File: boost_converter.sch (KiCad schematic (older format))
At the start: 12 parts

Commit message: small updates
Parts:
- removed R?: R, symbol R
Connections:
- net Control_OUT1 renamed Control_OUT
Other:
- moved on the sheet: R?
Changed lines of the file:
@@
 LIBS:power
 LIBS:device
-LIBS:switches
-LIBS:relays
-LIBS:motors
-LIBS:transistors
-LIBS:conn
 LIBS:linear
 LIBS:regul
-LIBS:74xx
-LIBS:cmos4000
 LIBS:adc-dac
 LIBS:memory
@@
 LIBS:digital-audio
 LIBS:philips
-LIBS:display
 LIBS:cypress
 LIBS:siliconi
@@
 LIBS:atmel
 LIBS:contrib
-LIBS:valves
 LIBS:lakotamm-microprocessors
 LIBS:lakotamm-powersupply
@@
 LIBS:lakotamm-transistor
 LIBS:lakotamm-wireless
+LIBS:MCU_ST_STM32
+LIBS:Transistor
+LIBS:Connector
 LIBS:F3K_Battery_manager-cache
 EELAYER 25 0
@@
 $EndComp
 Wire Wire Line
-	5850 4450 5850 4550
+	5850 4450 5850 4500
+Wire Wire Line
+	5850 4500 5850 4550
 Wire Wire Line
 	5750 4450 5750 4500
@@
 	6850 4150 6850 4200
 Wire Wire Line
-	6850 3750 6850 3850
+	6850 3750 6850 3800
+Wire Wire Line
+	6850 3800 6850 3850
 Wire Wire Line
 	6850 3350 6850 3450
 Wire Wire Line
-	6400 3350 8300 3350
+	6400 3350 6550 3350
+Wire Wire Line
+	6550 3350 6850 3350
+Wire Wire Line
+	6850 3350 8200 3350
+Wire Wire Line
+	8200 3350 8300 3350
 Connection ~ 6850 3800
 Wire Wire Line
@@
 Connection ~ 8200 3350
 Wire Wire Line
-	3650 3550 5200 3550
+	3650 3550 3800 3550
+Wire Wire Line
+	3800 3550 4550 3550
+Wire Wire Line
+	4550 3550 4850 3550
+Wire Wire Line
+	4850 3550 5200 3550
 Wire Wire Line
 	3800 3550 3800 3700
@@
 	4850 3900 4850 3950
 Wire Wire Line
-	4650 3950 5200 3950
+	4650 3950 4850 3950
+Wire Wire Line
+	4850 3950 5200 3950
 $Comp
 L R R?
 U 1 1 5AA41C36
-P 7200 3600
-F 0 "R?" V 7280 3600 50  0000 C CNN
-F 1 "R" V 7200 3600 50  0000 C CNN
-F 2 "" V 7130 3600 50  0001 C CNN
-F 3 "" H 7200 3600 50  0001 C CNN
-	1    7200 3600
-	0    1    1    0
-$EndComp
-$Comp
-L R R?
-U 1 1 5AA41D55
 P 7200 3800
 F 0 "R?" V 7280 3800 50  0000 C CNN
@@
 $EndComp
 Wire Wire Line
-	7050 3600 7000 3600
-Wire Wire Line
-	7000 3600 7000 4000
-Wire Wire Line
-	6400 3800 7050 3800
-Text HLabel 7400 3600 2    60   Input ~ 0
-Control_OUT1
+	7050 3800 7000 3800
+Wire Wire Line
+	7000 3800 7000 3800
+Wire Wire Line
+	7000 3800 7000 4000
 Text HLabel 7400 3800 2    60   Input ~ 0
-Control_OUT2
+Control_OUT
 Wire Wire Line
 	7350 3800 7400 3800
-Wire Wire Line
-	7350 3600 7400 3600
 Text HLabel 4650 3950 0    60   Input ~ 0
 ENA
@@
 $EndComp
 Wire Wire Line
-	4650 4100 5200 4100
+	4650 4100 4750 4100
+Wire Wire Line
+	4750 4100 5000 4100
+Wire Wire Line
+	5000 4100 5200 4100
 Wire Wire Line
 	5000 4100 5000 4200
@@
 Wire Wire Line
 	7000 4000 7400 4000
+Wire Wire Line
+	6400 3800 6550 3800
+Wire Wire Line
+	6550 3800 6850 3800
+Wire Wire Line
+	6850 3800 7000 3800
 $EndSCHEMATC

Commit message: added few MPNs
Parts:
- C15: renamed from C?; value 15uF -> 15uF 4V; footprint (none) -> Capacitors_SMD:C_0603; MPN (none) -> C1608X5R0G156M080AA
- C18: renamed from C?; value 33uF -> 33uF 4V; MPN (none) -> GRM21BR60G336ME15L
- L1: renamed from L?; MPN (none) -> IHLP1212BZER1R0M11
- R10: renamed from R?; value R -> 1M
- gave numbers to parts that had none: 7
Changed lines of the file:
@@
 $EndDescr
 $Comp
-L TPS61236P U?
+L TPS61236P U4
 U 1 1 5AA40BBB
 P 5800 3650
-F 0 "U?" H 6150 4100 60  0000 C CNN
+F 0 "U4" H 6150 4100 60  0000 C CNN
 F 1 "TPS61236P" H 5600 4100 60  0000 C CNN
 F 2 "" H 6050 4000 60  0001 C CNN
@@
 $EndComp
 $Comp
-L L L?
+L L L1
 U 1 1 5AA40C48
 P 4850 3350
-F 0 "L?" V 4800 3350 50  0000 C CNN
+F 0 "L1" V 4800 3350 50  0000 C CNN
 F 1 "1.2 uH 18mOhm" V 4925 3350 50  0000 C CNN
 F 2 "" H 4850 3350 50  0001 C CNN
 F 3 "" H 4850 3350 50  0001 C CNN
+F 4 "IHLP1212BZER1R0M11" V 4850 3350 60  0001 C CNN "MPN"
 	1    4850 3350
 	0    -1   -1   0
@@
 NoConn ~ 6400 4100
 $Comp
-L C C?
+L C C17
 U 1 1 5AA40CF8
 P 6550 3550
-F 0 "C?" H 6575 3650 50  0000 L CNN
+F 0 "C17" H 6575 3650 50  0000 L CNN
 F 1 "10pF" H 6575 3450 50  0000 L CNN
 F 2 "" H 6588 3400 50  0001 C CNN
@@
 $EndComp
 $Comp
-L R R?
+L R R11
 U 1 1 5AA40DAF
 P 6850 3600
-F 0 "R?" V 6930 3600 50  0000 C CNN
+F 0 "R11" V 6930 3600 50  0000 C CNN
 F 1 "R" V 6850 3600 50  0000 C CNN
 F 2 "" V 6780 3600 50  0001 C CNN
@@
 $EndComp
 $Comp
-L R R?
+L R R12
 U 1 1 5AA40DF4
 P 6850 4000
-F 0 "R?" V 6930 4000 50  0000 C CNN
+F 0 "R12" V 6930 4000 50  0000 C CNN
 F 1 "R" V 6850 4000 50  0000 C CNN
 F 2 "" V 6780 4000 50  0001 C CNN
@@
 $EndComp
 $Comp
-L GND #PWR?
+L GND #PWR49
 U 1 1 5AA40E28
 P 6850 4200
-F 0 "#PWR?" H 6850 3950 50  0001 C CNN
+F 0 "#PWR49" H 6850 3950 50  0001 C CNN
 F 1 "GND" H 6850 4050 50  0000 C CNN
 F 2 "" H 6850 4200 50  0001 C CNN
@@
 $EndComp
 $Comp
-L GND #PWR?
+L GND #PWR48
 U 1 1 5AA40E49
 P 5850 4550
-F 0 "#PWR?" H 5850 4300 50  0001 C CNN
+F 0 "#PWR48" H 5850 4300 50  0001 C CNN
 F 1 "GND" H 5850 4400 50  0000 C CNN
 F 2 "" H 5850 4550 50  0001 C CNN
@@
 $EndComp
 $Comp
-L C C?
+L C C18
 U 1 1 5AA40FA0
 P 8200 3800
-F 0 "C?" H 8225 3900 50  0000 L CNN
-F 1 "33uF" H 8225 3700 50  0000 L CNN
+F 0 "C18" H 8225 3900 50  0000 L CNN
+F 1 "33uF 4V" H 8250 3700 50  0000 L CNN
 F 2 "" H 8238 3650 50  0001 C CNN
 F 3 "" H 8200 3800 50  0001 C CNN
+F 4 "GRM21BR60G336ME15L" H 8200 3800 60  0001 C CNN "MPN"
 	1    8200 3800
 	1    0    0    -1
 $EndComp
 $Comp
-L GND #PWR?
+L GND #PWR50
 U 1 1 5AA40FE1
 P 8200 4200
-F 0 "#PWR?" H 8200 3950 50  0001 C CNN
+F 0 "#PWR50" H 8200 3950 50  0001 C CNN
 F 1 "GND" H 8200 4050 50  0000 C CNN
 F 2 "" H 8200 4200 50  0001 C CNN
@@
 VOUT
 $Comp
-L C C?
+L C C15
 U 1 1 5AA411D9
 P 3800 3850
-F 0 "C?" H 3825 3950 50  0000 L CNN
-F 1 "15uF" H 3825 3750 50  0000 L CNN
-F 2 "" H 3838 3700 50  0001 C CNN
+F 0 "C15" H 3825 3950 50  0000 L CNN
+F 1 "15uF 4V" H 3825 3750 50  0000 L CNN
+F 2 "Capacitors_SMD:C_0603" H 3838 3700 50  0001 C CNN
 F 3 "" H 3800 3850 50  0001 C CNN
+F 4 "C1608X5R0G156M080AA" H 3800 3850 60  0001 C CNN "MPN"
 	1    3800 3850
 	1    0    0    -1
 $EndComp
 $Comp
-L GND #PWR?
+L GND #PWR45
 U 1 1 5AA412DC
 P 3800 4200
-F 0 "#PWR?" H 3800 3950 50  0001 C CNN
+F 0 "#PWR45" H 3800 3950 50  0001 C CNN
 F 1 "GND" H 3800 4050 50  0000 C CNN
 F 2 "" H 3800 4200 50  0001 C CNN
@@
 $EndComp
 $Comp
-L R R?
+L R R10
 U 1 1 5AA417A7
 P 4850 3750
-F 0 "R?" V 4930 3750 50  0000 C CNN
-F 1 "R" V 4850 3750 50  0000 C CNN
+F 0 "R10" V 4930 3750 50  0000 C CNN
+F 1 "1M" V 4850 3750 50  0000 C CNN
 F 2 "" V 4780 3750 50  0001 C CNN
 F 3 "" H 4850 3750 50  0001 C CNN
@@
 $EndComp
 Wire Wire Line
-	5850 4450 5850 4500
-Wire Wire Line
-	5850 4500 5850 4550
+	5850 4450 5850 4550
 Wire Wire Line
 	5750 4450 5750 4500
@@
 	6850 4150 6850 4200
 Wire Wire Line
-	6850 3750 6850 3800
-Wire Wire Line
-	6850 3800 6850 3850
+	6850 3750 6850 3850
 Wire Wire Line
 	6850 3350 6850 3450
 Wire Wire Line
-	6400 3350 6550 3350
-Wire Wire Line
-	6550 3350 6850 3350
-Wire Wire Line
-	6850 3350 8200 3350
-Wire Wire Line
-	8200 3350 8300 3350
+	6400 3350 8300 3350
 Connection ~ 6850 3800
 Wire Wire Line
@@
 Connection ~ 8200 3350
 Wire Wire Line
-	3650 3550 3800 3550
-Wire Wire Line
-	3800 3550 4550 3550
-Wire Wire Line
-	4550 3550 4850 3550
-Wire Wire Line
-	4850 3550 5200 3550
+	3650 3550 5200 3550
 Wire Wire Line
 	3800 3550 3800 3700
@@
 	4850 3900 4850 3950
 Wire Wire Line
-	4650 3950 4850 3950
-Wire Wire Line
-	4850 3950 5200 3950
-$Comp
-L R R?
+	4650 3950 5200 3950
+$Comp
+L R R13
 U 1 1 5AA41C36
 P 7200 3800
-F 0 "R?" V 7280 3800 50  0000 C CNN
+F 0 "R13" V 7280 3800 50  0000 C CNN
 F 1 "R" V 7200 3800 50  0000 C CNN
 F 2 "" V 7130 3800 50  0001 C CNN
@@
 $EndComp
 Wire Wire Line
-	7050 3800 7000 3800
-Wire Wire Line
-	7000 3800 7000 3800
+	6400 3800 7050 3800
 Wire Wire Line
 	7000 3800 7000 4000
@@
 Connection ~ 4850 3950
 $Comp
-L +BATT #PWR?
+L +BATT #PWR44
 U 1 1 5AA423A0
 P 3650 3450
-F 0 "#PWR?" H 3650 3300 50  0001 C CNN
+F 0 "#PWR44" H 3650 3300 50  0001 C CNN
 F 1 "+BATT" H 3650 3590 50  0000 C CNN
 F 2 "" H 3650 3450 50  0001 C CNN
@@
 Connection ~ 3800 3550
 $Comp
-L C C?
+L C C16
 U 1 1 5AA42591
 P 5000 4350
-F 0 "C?" H 5025 4450 50  0000 L CNN
+F 0 "C16" H 5025 4450 50  0000 L CNN
 F 1 "10nF" H 5025 4250 50  0000 L CNN
 F 2 "" H 5038 4200 50  0001 C CNN
@@
 $EndComp
 $Comp
-L R R?
+L R R9
 U 1 1 5AA425EF
 P 4750 4350
-F 0 "R?" V 4830 4350 50  0000 C CNN
+F 0 "R9" V 4830 4350 50  0000 C CNN
 F 1 "R" V 4750 4350 50  0000 C CNN
 F 2 "" V 4680 4350 50  0001 C CNN
@@
 $EndComp
 Wire Wire Line
-	4650 4100 4750 4100
-Wire Wire Line
-	4750 4100 5000 4100
-Wire Wire Line
-	5000 4100 5200 4100
+	4650 4100 5200 4100
 Wire Wire Line
 	5000 4100 5000 4200
@@
 Connection ~ 5000 4100
 $Comp
-L GND #PWR?
+L GND #PWR47
 U 1 1 5AA42711
 P 5000 4550
-F 0 "#PWR?" H 5000 4300 50  0001 C CNN
+F 0 "#PWR47" H 5000 4300 50  0001 C CNN
 F 1 "GND" H 5000 4400 50  0000 C CNN
 F 2 "" H 5000 4550 50  0001 C CNN
@@
 	5000 4500 5000 4550
 $Comp
-L GND #PWR?
+L GND #PWR46
 U 1 1 5AA42804
 P 4750 4550
-F 0 "#PWR?" H 4750 4300 50  0001 C CNN
+F 0 "#PWR46" H 4750 4300 50  0001 C CNN
 F 1 "GND" H 4750 4400 50  0000 C CNN
 F 2 "" H 4750 4550 50  0001 C CNN
@@
 Wire Wire Line
 	7000 4000 7400 4000
-Wire Wire Line
-	6400 3800 6550 3800
-Wire Wire Line
-	6550 3800 6850 3800
-Wire Wire Line
-	6850 3800 7000 3800
 $EndSCHEMATC

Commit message: Progress on the charging circuit
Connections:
- net Control_OUT renamed Voltage_control
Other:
- moved on the sheet: C18
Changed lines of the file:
@@
 $Descr A4 11693 8268
 encoding utf-8
-Sheet 4 4
+Sheet 3 4
 Title ""
 Date ""
@@
 L C C18
 U 1 1 5AA40FA0
-P 8200 3800
-F 0 "C18" H 8225 3900 50  0000 L CNN
-F 1 "33uF 4V" H 8250 3700 50  0000 L CNN
-F 2 "" H 8238 3650 50  0001 C CNN
-F 3 "" H 8200 3800 50  0001 C CNN
-F 4 "GRM21BR60G336ME15L" H 8200 3800 60  0001 C CNN "MPN"
-	1    8200 3800
+P 8300 3800
+F 0 "C18" H 8325 3900 50  0000 L CNN
+F 1 "33uF 4V" H 8350 3700 50  0000 L CNN
+F 2 "" H 8338 3650 50  0001 C CNN
+F 3 "" H 8300 3800 50  0001 C CNN
+F 4 "GRM21BR60G336ME15L" H 8300 3800 60  0001 C CNN "MPN"
+	1    8300 3800
 	1    0    0    -1
 $EndComp
@@
 L GND #PWR50
 U 1 1 5AA40FE1
-P 8200 4200
-F 0 "#PWR50" H 8200 3950 50  0001 C CNN
-F 1 "GND" H 8200 4050 50  0000 C CNN
-F 2 "" H 8200 4200 50  0001 C CNN
-F 3 "" H 8200 4200 50  0001 C CNN
-	1    8200 4200
-	1    0    0    -1
-$EndComp
-Text HLabel 8300 3350 2    60   Output ~ 0
+P 8300 4200
+F 0 "#PWR50" H 8300 3950 50  0001 C CNN
+F 1 "GND" H 8300 4050 50  0000 C CNN
+F 2 "" H 8300 4200 50  0001 C CNN
+F 3 "" H 8300 4200 50  0001 C CNN
+	1    8300 4200
+	1    0    0    -1
+$EndComp
+Text HLabel 8400 3350 2    60   Output ~ 0
 VOUT
 $Comp
@@
 $EndComp
 Wire Wire Line
-	5850 4450 5850 4550
+	5850 4450 5850 4500
+Wire Wire Line
+	5850 4500 5850 4550
 Wire Wire Line
 	5750 4450 5750 4500
@@
 	6850 4150 6850 4200
 Wire Wire Line
-	6850 3750 6850 3850
+	6850 3750 6850 3800
+Wire Wire Line
+	6850 3800 6850 3850
 Wire Wire Line
 	6850 3350 6850 3450
 Wire Wire Line
-	6400 3350 8300 3350
+	6400 3350 6550 3350
+Wire Wire Line
+	6550 3350 6850 3350
+Wire Wire Line
+	6850 3350 8300 3350
+Wire Wire Line
+	8300 3350 8400 3350
 Connection ~ 6850 3800
 Wire Wire Line
@@
 Connection ~ 6550 3350
 Wire Wire Line
-	8200 3350 8200 3650
+	8300 3350 8300 3650
 Connection ~ 6850 3350
 Wire Wire Line
-	8200 3950 8200 4200
-Connection ~ 8200 3350
-Wire Wire Line
-	3650 3550 5200 3550
+	8300 3950 8300 4200
+Connection ~ 8300 3350
+Wire Wire Line
+	3650 3550 3800 3550
+Wire Wire Line
+	3800 3550 4550 3550
+Wire Wire Line
+	4550 3550 4850 3550
+Wire Wire Line
+	4850 3550 5200 3550
 Wire Wire Line
 	3800 3550 3800 3700
@@
 	4850 3900 4850 3950
 Wire Wire Line
-	4650 3950 5200 3950
+	4650 3950 4850 3950
+Wire Wire Line
+	4850 3950 5200 3950
 $Comp
 L R R13
@@
 $EndComp
 Wire Wire Line
-	6400 3800 7050 3800
+	6400 3800 6550 3800
+Wire Wire Line
+	6550 3800 6850 3800
+Wire Wire Line
+	6850 3800 7000 3800
+Wire Wire Line
+	7000 3800 7050 3800
 Wire Wire Line
 	7000 3800 7000 4000
 Text HLabel 7400 3800 2    60   Input ~ 0
-Control_OUT
+Voltage_control
 Wire Wire Line
 	7350 3800 7400 3800
@@
 $EndComp
 Wire Wire Line
-	4650 4100 5200 4100
+	4650 4100 4750 4100
+Wire Wire Line
+	4750 4100 5000 4100
+Wire Wire Line
+	5000 4100 5200 4100
 Wire Wire Line
 	5000 4100 5000 4200

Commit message: Updated MCU pinout
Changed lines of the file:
@@
 $EndComp
 Wire Wire Line
-	5850 4450 5850 4500
-Wire Wire Line
-	5850 4500 5850 4550
+	5850 4450 5850 4550
 Wire Wire Line
 	5750 4450 5750 4500
@@
 	6850 4150 6850 4200
 Wire Wire Line
-	6850 3750 6850 3800
-Wire Wire Line
-	6850 3800 6850 3850
+	6850 3750 6850 3850
 Wire Wire Line
 	6850 3350 6850 3450
 Wire Wire Line
-	6400 3350 6550 3350
-Wire Wire Line
-	6550 3350 6850 3350
-Wire Wire Line
-	6850 3350 8300 3350
-Wire Wire Line
-	8300 3350 8400 3350
+	6400 3350 8400 3350
 Connection ~ 6850 3800
 Wire Wire Line
@@
 Connection ~ 8300 3350
 Wire Wire Line
-	3650 3550 3800 3550
-Wire Wire Line
-	3800 3550 4550 3550
-Wire Wire Line
-	4550 3550 4850 3550
-Wire Wire Line
-	4850 3550 5200 3550
+	3650 3550 5200 3550
 Wire Wire Line
 	3800 3550 3800 3700
@@
 	4850 3900 4850 3950
 Wire Wire Line
-	4650 3950 4850 3950
-Wire Wire Line
-	4850 3950 5200 3950
+	4650 3950 5200 3950
 $Comp
 L R R13
@@
 $EndComp
 Wire Wire Line
-	6400 3800 6550 3800
-Wire Wire Line
-	6550 3800 6850 3800
-Wire Wire Line
-	6850 3800 7000 3800
-Wire Wire Line
-	7000 3800 7050 3800
+	6400 3800 7050 3800
 Wire Wire Line
 	7000 3800 7000 4000
@@
 $EndComp
 Wire Wire Line
-	4650 4100 4750 4100
-Wire Wire Line
-	4750 4100 5000 4100
-Wire Wire Line
-	5000 4100 5200 4100
+	4650 4100 5200 4100
 Wire Wire Line
 	5000 4100 5000 4200

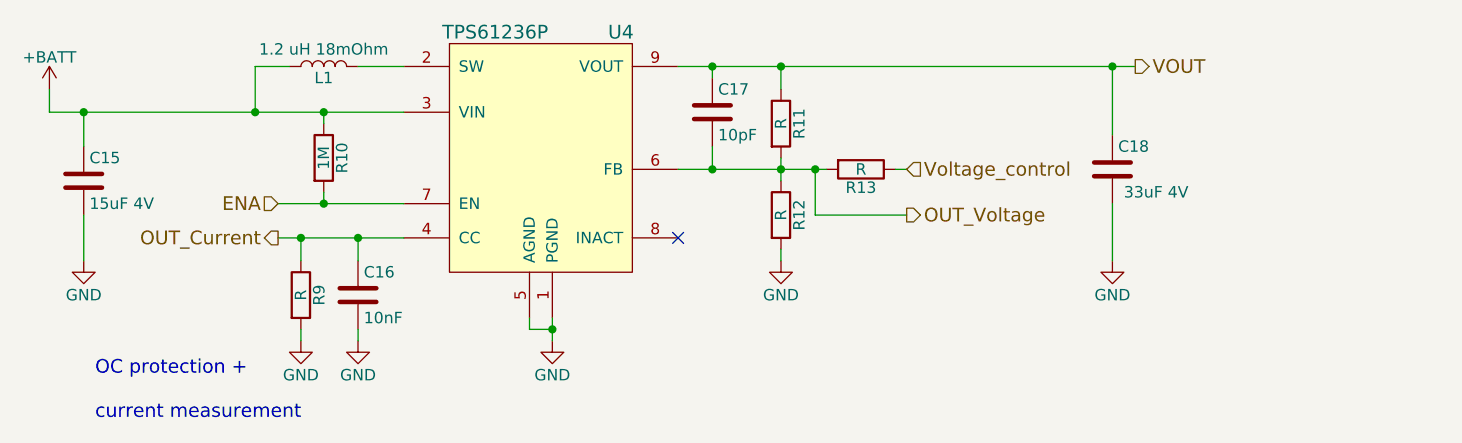
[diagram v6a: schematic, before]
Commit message: Simplified schematic, changed pinout
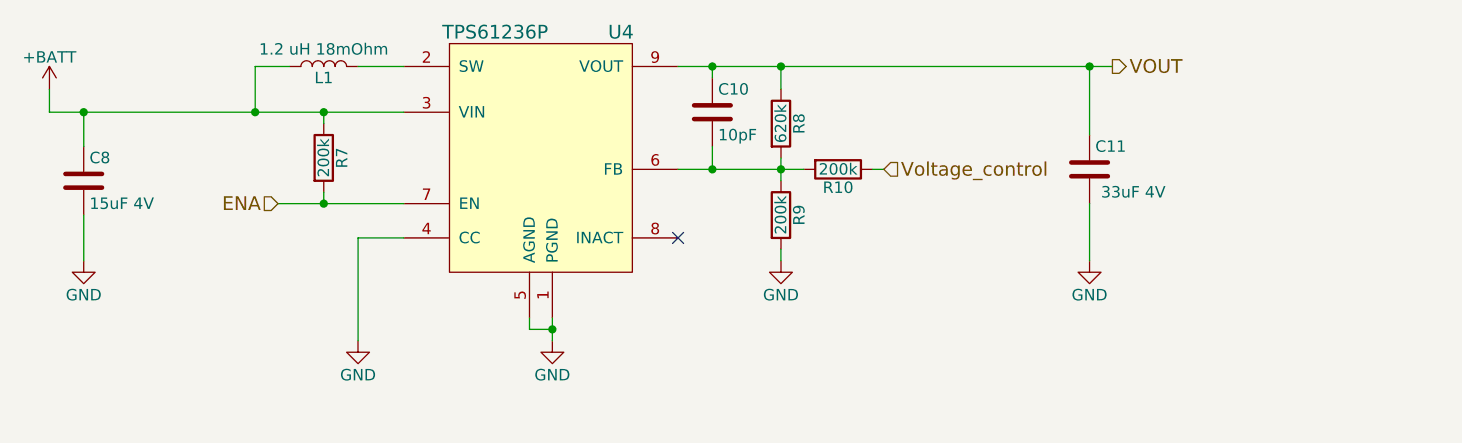
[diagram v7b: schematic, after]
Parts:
- removed C16: 10nF, symbol C
- removed R9: R, symbol R
- R10: renamed from R13; value R -> 200k; footprint (none) -> Resistors_SMD:R_0402
- R7: renamed from R10; value 1M -> 200k; footprint (none) -> Resistors_SMD:R_0402
- R8: renamed from R11; value R -> 620k; footprint (none) -> Resistors_SMD:R_0402
- R9: renamed from R12; value R -> 200k; footprint (none) -> Resistors_SMD:R_0402
- renumbered C17 to C10, C18 to C11, C15 to C8
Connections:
- net OUT_Current is gone; now on net GND: U4.4 (CC)
- net OUT_Voltage: no longer names the net of C10.2, R10.2, R8.2, R9.1, U4.6 (FB)
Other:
- note removed: "OC protection +\n\ncurrent measurement\n"
- moved on the sheet: C11, R10
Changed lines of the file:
@@
 NoConn ~ 6400 4100
 $Comp
-L C C17
+L C C10
 U 1 1 5AA40CF8
 P 6550 3550
-F 0 "C17" H 6575 3650 50  0000 L CNN
+F 0 "C10" H 6575 3650 50  0000 L CNN
 F 1 "10pF" H 6575 3450 50  0000 L CNN
 F 2 "" H 6588 3400 50  0001 C CNN
@@
 $EndComp
 $Comp
-L R R11
+L R R8
 U 1 1 5AA40DAF
 P 6850 3600
-F 0 "R11" V 6930 3600 50  0000 C CNN
-F 1 "R" V 6850 3600 50  0000 C CNN
-F 2 "" V 6780 3600 50  0001 C CNN
+F 0 "R8" V 6930 3600 50  0000 C CNN
+F 1 "620k" V 6850 3600 50  0000 C CNN
+F 2 "Resistors_SMD:R_0402" V 6780 3600 50  0001 C CNN
 F 3 "" H 6850 3600 50  0001 C CNN
 	1    6850 3600
@@
 $EndComp
 $Comp
-L R R12
+L R R9
 U 1 1 5AA40DF4
 P 6850 4000
-F 0 "R12" V 6930 4000 50  0000 C CNN
-F 1 "R" V 6850 4000 50  0000 C CNN
-F 2 "" V 6780 4000 50  0001 C CNN
+F 0 "R9" V 6930 4000 50  0000 C CNN
+F 1 "200k" V 6850 4000 50  0000 C CNN
+F 2 "Resistors_SMD:R_0402" V 6780 4000 50  0001 C CNN
 F 3 "" H 6850 4000 50  0001 C CNN
 	1    6850 4000
@@
 $EndComp
 $Comp
-L GND #PWR49
+L GND #PWR032
 U 1 1 5AA40E28
 P 6850 4200
-F 0 "#PWR49" H 6850 3950 50  0001 C CNN
+F 0 "#PWR032" H 6850 3950 50  0001 C CNN
 F 1 "GND" H 6850 4050 50  0000 C CNN
 F 2 "" H 6850 4200 50  0001 C CNN
@@
 $EndComp
 $Comp
-L GND #PWR48
+L GND #PWR033
 U 1 1 5AA40E49
 P 5850 4550
-F 0 "#PWR48" H 5850 4300 50  0001 C CNN
+F 0 "#PWR033" H 5850 4300 50  0001 C CNN
 F 1 "GND" H 5850 4400 50  0000 C CNN
 F 2 "" H 5850 4550 50  0001 C CNN
@@
 $EndComp
 $Comp
-L C C18
+L C C11
 U 1 1 5AA40FA0
-P 8300 3800
-F 0 "C18" H 8325 3900 50  0000 L CNN
-F 1 "33uF 4V" H 8350 3700 50  0000 L CNN
-F 2 "" H 8338 3650 50  0001 C CNN
-F 3 "" H 8300 3800 50  0001 C CNN
-F 4 "GRM21BR60G336ME15L" H 8300 3800 60  0001 C CNN "MPN"
-	1    8300 3800
-	1    0    0    -1
-$EndComp
-$Comp
-L GND #PWR50
+P 8200 3800
+F 0 "C11" H 8225 3900 50  0000 L CNN
+F 1 "33uF 4V" H 8250 3700 50  0000 L CNN
+F 2 "" H 8238 3650 50  0001 C CNN
+F 3 "" H 8200 3800 50  0001 C CNN
+F 4 "GRM21BR60G336ME15L" H 8200 3800 60  0001 C CNN "MPN"
+	1    8200 3800
+	1    0    0    -1
+$EndComp
+$Comp
+L GND #PWR034
 U 1 1 5AA40FE1
-P 8300 4200
-F 0 "#PWR50" H 8300 3950 50  0001 C CNN
-F 1 "GND" H 8300 4050 50  0000 C CNN
-F 2 "" H 8300 4200 50  0001 C CNN
-F 3 "" H 8300 4200 50  0001 C CNN
-	1    8300 4200
-	1    0    0    -1
-$EndComp
-Text HLabel 8400 3350 2    60   Output ~ 0
+P 8200 4200
+F 0 "#PWR034" H 8200 3950 50  0001 C CNN
+F 1 "GND" H 8200 4050 50  0000 C CNN
+F 2 "" H 8200 4200 50  0001 C CNN
+F 3 "" H 8200 4200 50  0001 C CNN
+	1    8200 4200
+	1    0    0    -1
+$EndComp
+Text HLabel 8300 3350 2    60   Output ~ 0
 VOUT
 $Comp
-L C C15
+L C C8
 U 1 1 5AA411D9
 P 3800 3850
-F 0 "C15" H 3825 3950 50  0000 L CNN
+F 0 "C8" H 3825 3950 50  0000 L CNN
 F 1 "15uF 4V" H 3825 3750 50  0000 L CNN
 F 2 "Capacitors_SMD:C_0603" H 3838 3700 50  0001 C CNN
@@
 $EndComp
 $Comp
-L GND #PWR45
+L GND #PWR035
 U 1 1 5AA412DC
 P 3800 4200
-F 0 "#PWR45" H 3800 3950 50  0001 C CNN
+F 0 "#PWR035" H 3800 3950 50  0001 C CNN
 F 1 "GND" H 3800 4050 50  0000 C CNN
 F 2 "" H 3800 4200 50  0001 C CNN
@@
 $EndComp
 $Comp
-L R R10
+L R R7
 U 1 1 5AA417A7
 P 4850 3750
-F 0 "R10" V 4930 3750 50  0000 C CNN
-F 1 "1M" V 4850 3750 50  0000 C CNN
-F 2 "" V 4780 3750 50  0001 C CNN
+F 0 "R7" V 4930 3750 50  0000 C CNN
+F 1 "200k" V 4850 3750 50  0000 C CNN
+F 2 "Resistors_SMD:R_0402" V 4780 3750 50  0001 C CNN
 F 3 "" H 4850 3750 50  0001 C CNN
 	1    4850 3750
@@
 	6850 3350 6850 3450
 Wire Wire Line
-	6400 3350 8400 3350
+	6400 3350 8300 3350
 Connection ~ 6850 3800
 Wire Wire Line
@@
 Connection ~ 6550 3350
 Wire Wire Line
-	8300 3350 8300 3650
+	8200 3350 8200 3650
 Connection ~ 6850 3350
 Wire Wire Line
-	8300 3950 8300 4200
-Connection ~ 8300 3350
+	8200 3950 8200 4200
+Connection ~ 8200 3350
 Wire Wire Line
 	3650 3550 5200 3550
@@
 	4650 3950 5200 3950
 $Comp
-L R R13
+L R R10
 U 1 1 5AA41C36
-P 7200 3800
-F 0 "R13" V 7280 3800 50  0000 C CNN
-F 1 "R" V 7200 3800 50  0000 C CNN
-F 2 "" V 7130 3800 50  0001 C CNN
-F 3 "" H 7200 3800 50  0001 C CNN
-	1    7200 3800
+P 7100 3800
+F 0 "R10" V 7180 3800 50  0000 C CNN
+F 1 "200k" V 7100 3800 50  0000 C CNN
+F 2 "Resistors_SMD:R_0402" V 7030 3800 50  0001 C CNN
+F 3 "" H 7100 3800 50  0001 C CNN
+	1    7100 3800
 	0    1    1    0
 $EndComp
 Wire Wire Line
-	6400 3800 7050 3800
-Wire Wire Line
-	7000 3800 7000 4000
-Text HLabel 7400 3800 2    60   Input ~ 0
+	6400 3800 6950 3800
+Text HLabel 7300 3800 2    60   Input ~ 0
 Voltage_control
 Wire Wire Line
-	7350 3800 7400 3800
+	7250 3800 7300 3800
 Text HLabel 4650 3950 0    60   Input ~ 0
 ENA
 Connection ~ 4850 3950
 $Comp
-L +BATT #PWR44
+L +BATT #PWR036
 U 1 1 5AA423A0
 P 3650 3450
-F 0 "#PWR44" H 3650 3300 50  0001 C CNN
+F 0 "#PWR036" H 3650 3300 50  0001 C CNN
 F 1 "+BATT" H 3650 3590 50  0000 C CNN
 F 2 "" H 3650 3450 50  0001 C CNN
@@
 Connection ~ 3800 3550
 $Comp
-L C C16
-U 1 1 5AA42591
-P 5000 4350
-F 0 "C16" H 5025 4450 50  0000 L CNN
-F 1 "10nF" H 5025 4250 50  0000 L CNN
-F 2 "" H 5038 4200 50  0001 C CNN
-F 3 "" H 5000 4350 50  0001 C CNN
-	1    5000 4350
-	1    0    0    -1
-$EndComp
-$Comp
-L R R9
-U 1 1 5AA425EF
-P 4750 4350
-F 0 "R9" V 4830 4350 50  0000 C CNN
-F 1 "R" V 4750 4350 50  0000 C CNN
-F 2 "" V 4680 4350 50  0001 C CNN
-F 3 "" H 4750 4350 50  0001 C CNN
-	1    4750 4350
-	1    0    0    -1
-$EndComp
-Wire Wire Line
-	4650 4100 5200 4100
-Wire Wire Line
-	5000 4100 5000 4200
-Wire Wire Line
-	4750 4200 4750 4100
-Connection ~ 5000 4100
-$Comp
-L GND #PWR47
+L GND #PWR037
 U 1 1 5AA42711
 P 5000 4550
-F 0 "#PWR47" H 5000 4300 50  0001 C CNN
+F 0 "#PWR037" H 5000 4300 50  0001 C CNN
 F 1 "GND" H 5000 4400 50  0000 C CNN
 F 2 "" H 5000 4550 50  0001 C CNN
@@
 $EndComp
 Wire Wire Line
-	5000 4500 5000 4550
-$Comp
-L GND #PWR46
-U 1 1 5AA42804
-P 4750 4550
-F 0 "#PWR46" H 4750 4300 50  0001 C CNN
-F 1 "GND" H 4750 4400 50  0000 C CNN
-F 2 "" H 4750 4550 50  0001 C CNN
-F 3 "" H 4750 4550 50  0001 C CNN
-	1    4750 4550
-	1    0    0    -1
-$EndComp
-Wire Wire Line
-	4750 4500 4750 4550
-Text Notes 3850 4900 0    60   ~ 0
-OC protection +\n\ncurrent measurement\n
-Text HLabel 4650 4100 0    60   Output ~ 0
-OUT_Current
-Connection ~ 4750 4100
-Connection ~ 7000 3800
-Text HLabel 7400 4000 2    60   Output ~ 0
-OUT_Voltage
-Wire Wire Line
-	7000 4000 7400 4000
+	5000 4100 5000 4550
+Wire Wire Line
+	5200 4100 5000 4100
 $EndSCHEMATC
